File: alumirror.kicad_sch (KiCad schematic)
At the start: 56 parts, among them SW00 PG1350, SW01 PG1350, SW02 PG1350, SW03 PG1350, SW04 PG1350, SW05 PG1350, SW10 PG1350, SW11 PG1350, SW12 PG1350, SW13 PG1350, SW14 PG1350, SW15 PG1350, SW20 PG1350, SW21 PG1350, SW22 PG1350, SW23 PG1350, SW24 PG1350, SW25 PG1350_1½U, SW30 PG1350_1½U, SW31 PG1350/SKQUCAA010, U1 CH552T, U2 CH552T

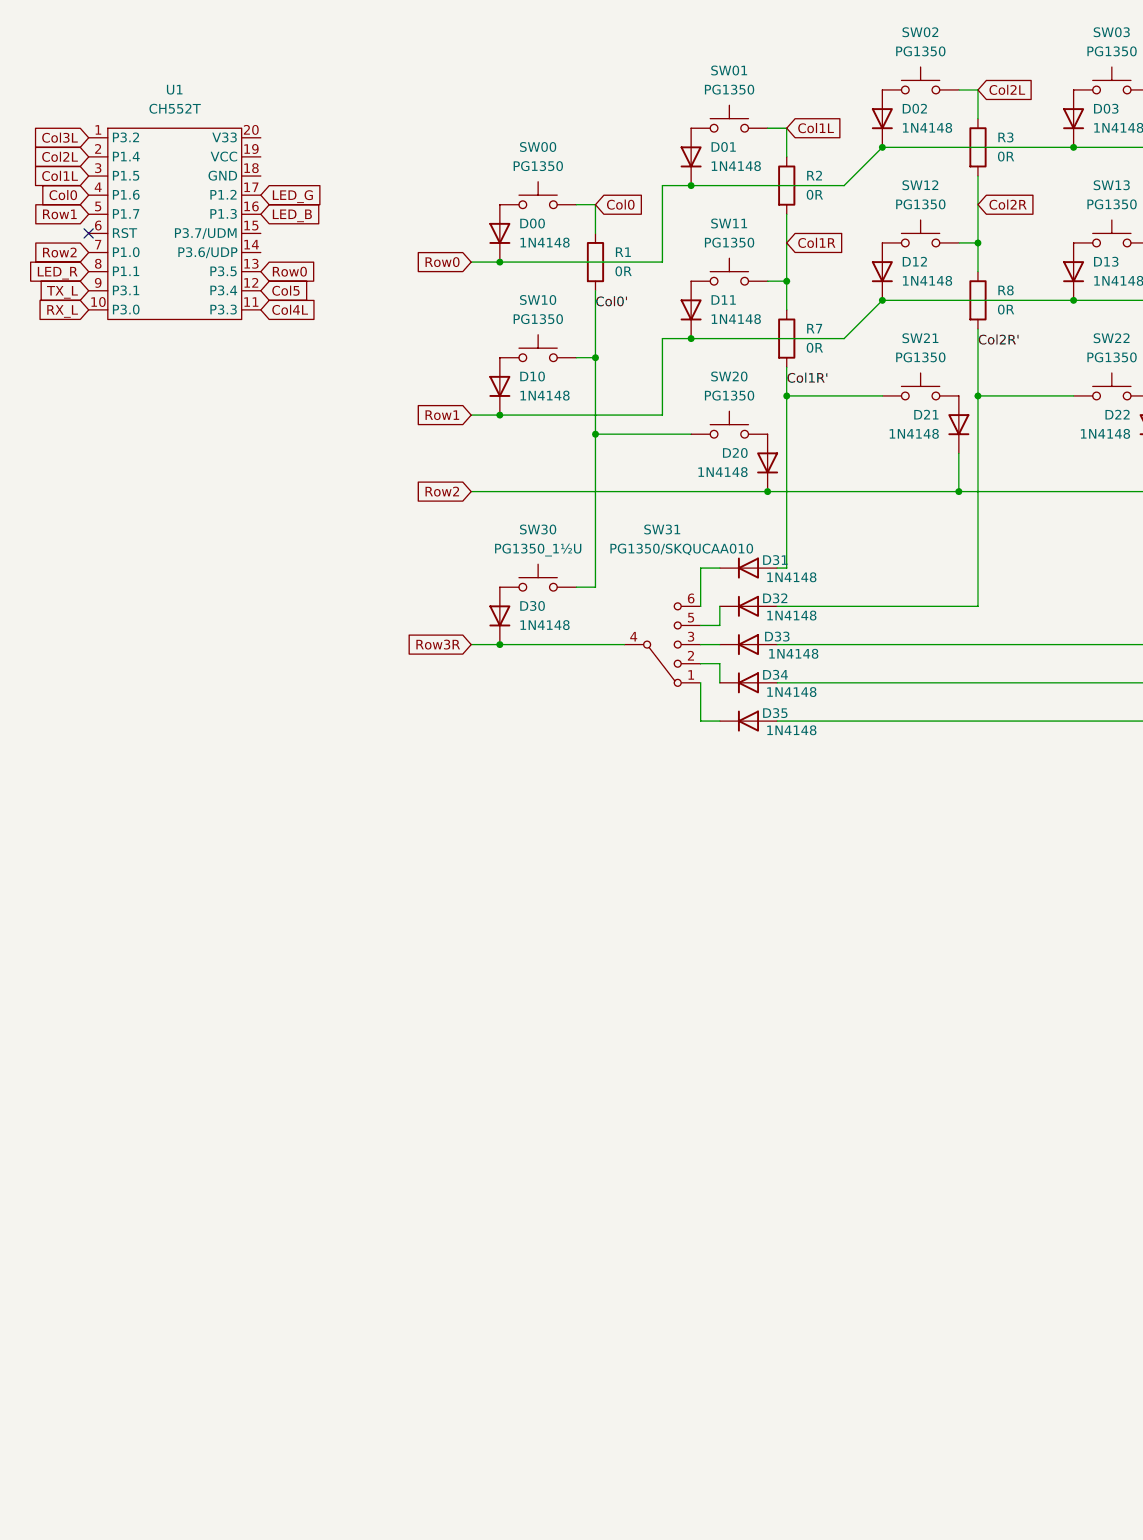
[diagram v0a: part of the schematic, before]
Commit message: Add lefthand USB, ESD, etc. components to schematic
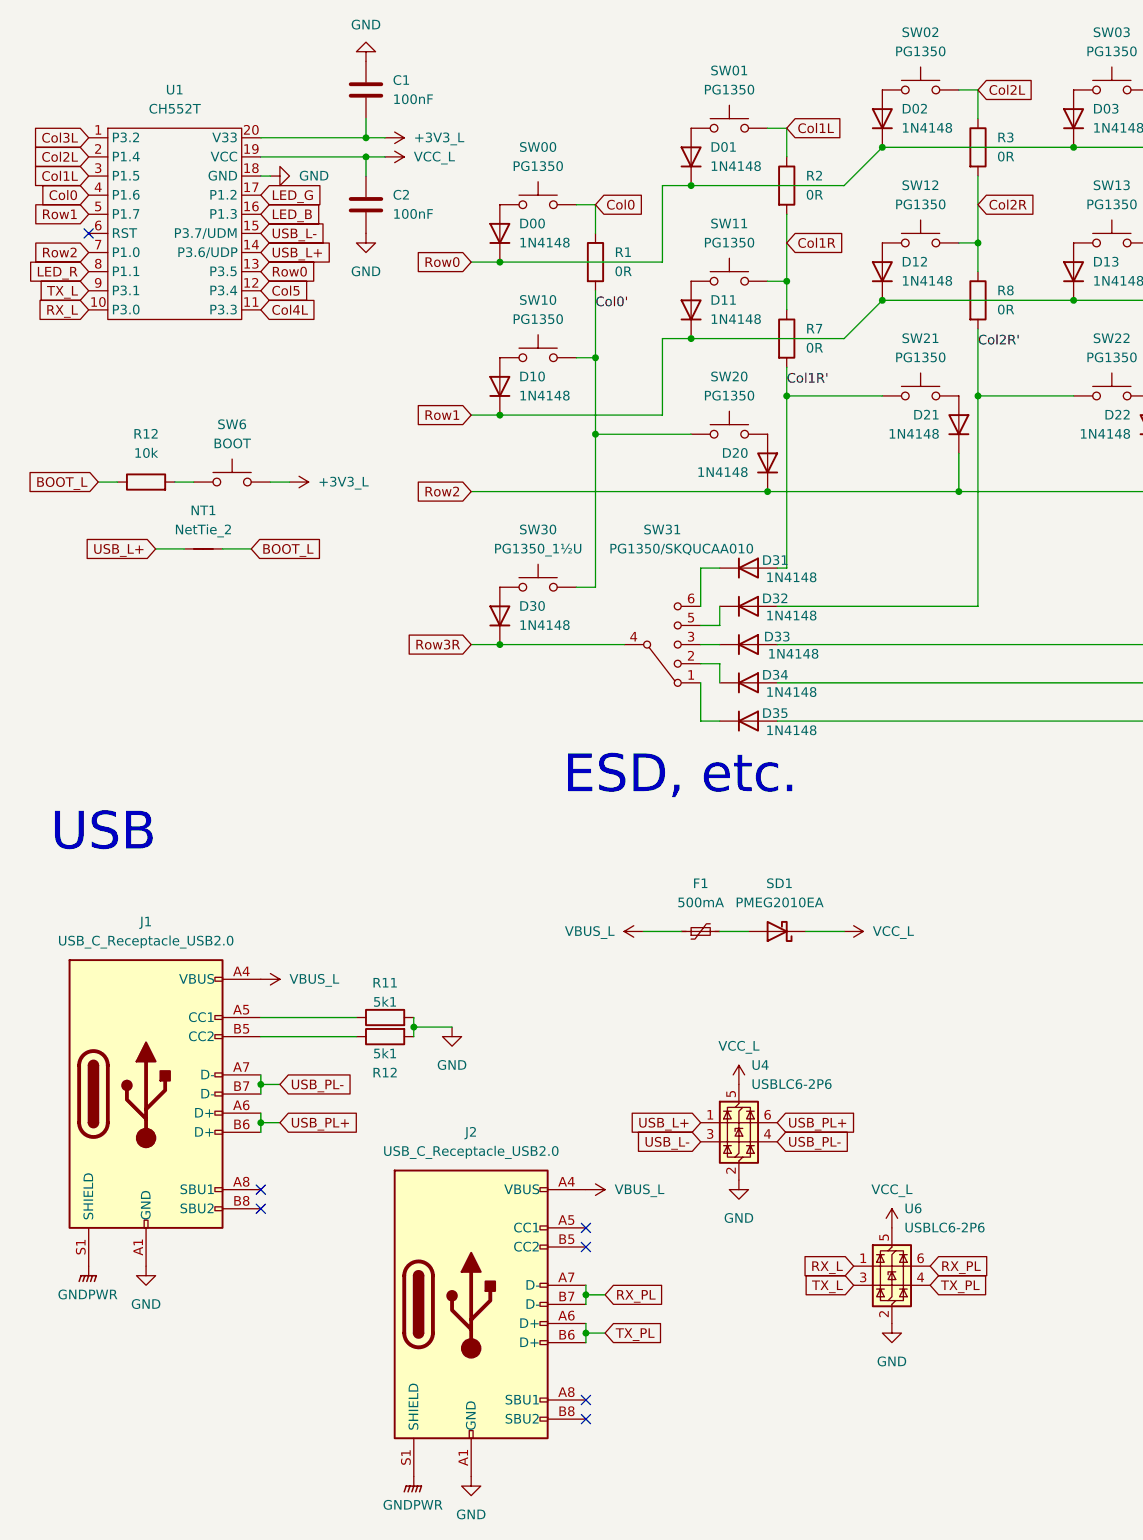
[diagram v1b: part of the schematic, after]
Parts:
- added C1, C2: 100nF, Capacitor_SMD:C_0603_1608Metric, symbol Device:C
- added F1: 500mA, Fuse:Fuse_0603_1608Metric, symbol Device:Polyfuse_Small
- added J1, J2: USB_C_Receptacle_USB2.0, Connector_USB:USB_C_Receptacle_GCT_USB4105-xx-A_16P_TopMnt_Horizontal, symbol Connector:USB_C_Receptacle_USB2.0
- added NT1: NetTie_2, Project Library:NetTie-2_SMD_Pad0.254mm, symbol Device:NetTie_2
- added R11, R12: 5k1, Resistor_SMD:R_0603_1608Metric, symbol Device:R
- added R12: 10k, Resistor_SMD:R_0603_1608Metric, symbol Device:R
- added SD1: PMEG2010EA, Diode_SMD:D_SOD-323, symbol Device:D_Schottky
- added SW6: BOOT, PCM_marbastlib-various:SW_SPST_SKQG_WithStem, symbol Switch:SW_Push
- added U4, U6: USBLC6-2P6, Package_TO_SOT_SMD:SOT-666, symbol Power_Protection:USBLC6-2P6
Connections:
- net RX_L: now also U6.1 (I/O1)
- net TX_L: now also U6.3 (I/O2)
- net USB_L+: now reaches U1.14 (P3.6/UDP)
- net USB_L+: now also NT1.2, U4.1 (I/O1)
- net USB_L-: now reaches U1.15 (P3.7/UDM)
- net USB_L-: now also U4.3 (I/O2)
- net GND: now reaches U1.18 (GND)
- net GND: now also C1.2, C2.2, J1.A1 (GND), J1.A12 (GND), J1.B1 (GND), J1.B12 (GND), J2.A1 (GND), J2.A12 (GND), J2.B1 (GND), J2.B12 (GND), R11.2, R12.2, U4.2 (GND), U6.2 (GND)
- net VCC_L: now reaches U1.19 (VCC)
- net VCC_L: now also C2.1, SD1.1 (K), U4.5 (VBUS), U6.5 (VBUS)
- net +3V3_L: now reaches U1.20 (V33)
- net +3V3_L: now also C1.1, SW6.2
- new net: F1.2, SD1.2 (A)
- new net: J1.A5 (CC1), R11.1
- new net: J1.B5 (CC2), R12.1
- new net: R12.2, SW6.1
- new net BOOT_L: NT1.1, R12.1
- new net GNDPWR: J1.S1 (SHIELD), J2.S1 (SHIELD)
- new net RX_PL: J2.A7 (D-), J2.B7 (D-), U6.6 (I/O1)
- new net TX_PL: J2.A6 (D+), J2.B6 (D+), U6.4 (I/O2)
- new net USB_PL+: J1.A6 (D+), J1.B6 (D+), U4.6 (I/O1)
- new net USB_PL-: J1.A7 (D-), J1.B7 (D-), U4.4 (I/O2)
- new net VBUS_L: F1.1, J1.A4 (VBUS), J1.A9 (VBUS), J1.B4 (VBUS), J1.B9 (VBUS), J2.A4 (VBUS), J2.A9 (VBUS), J2.B4 (VBUS), J2.B9 (VBUS)
- no-connect marks 2 -> 8
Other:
- note added: "ESD, etc."
- note added: "USB"

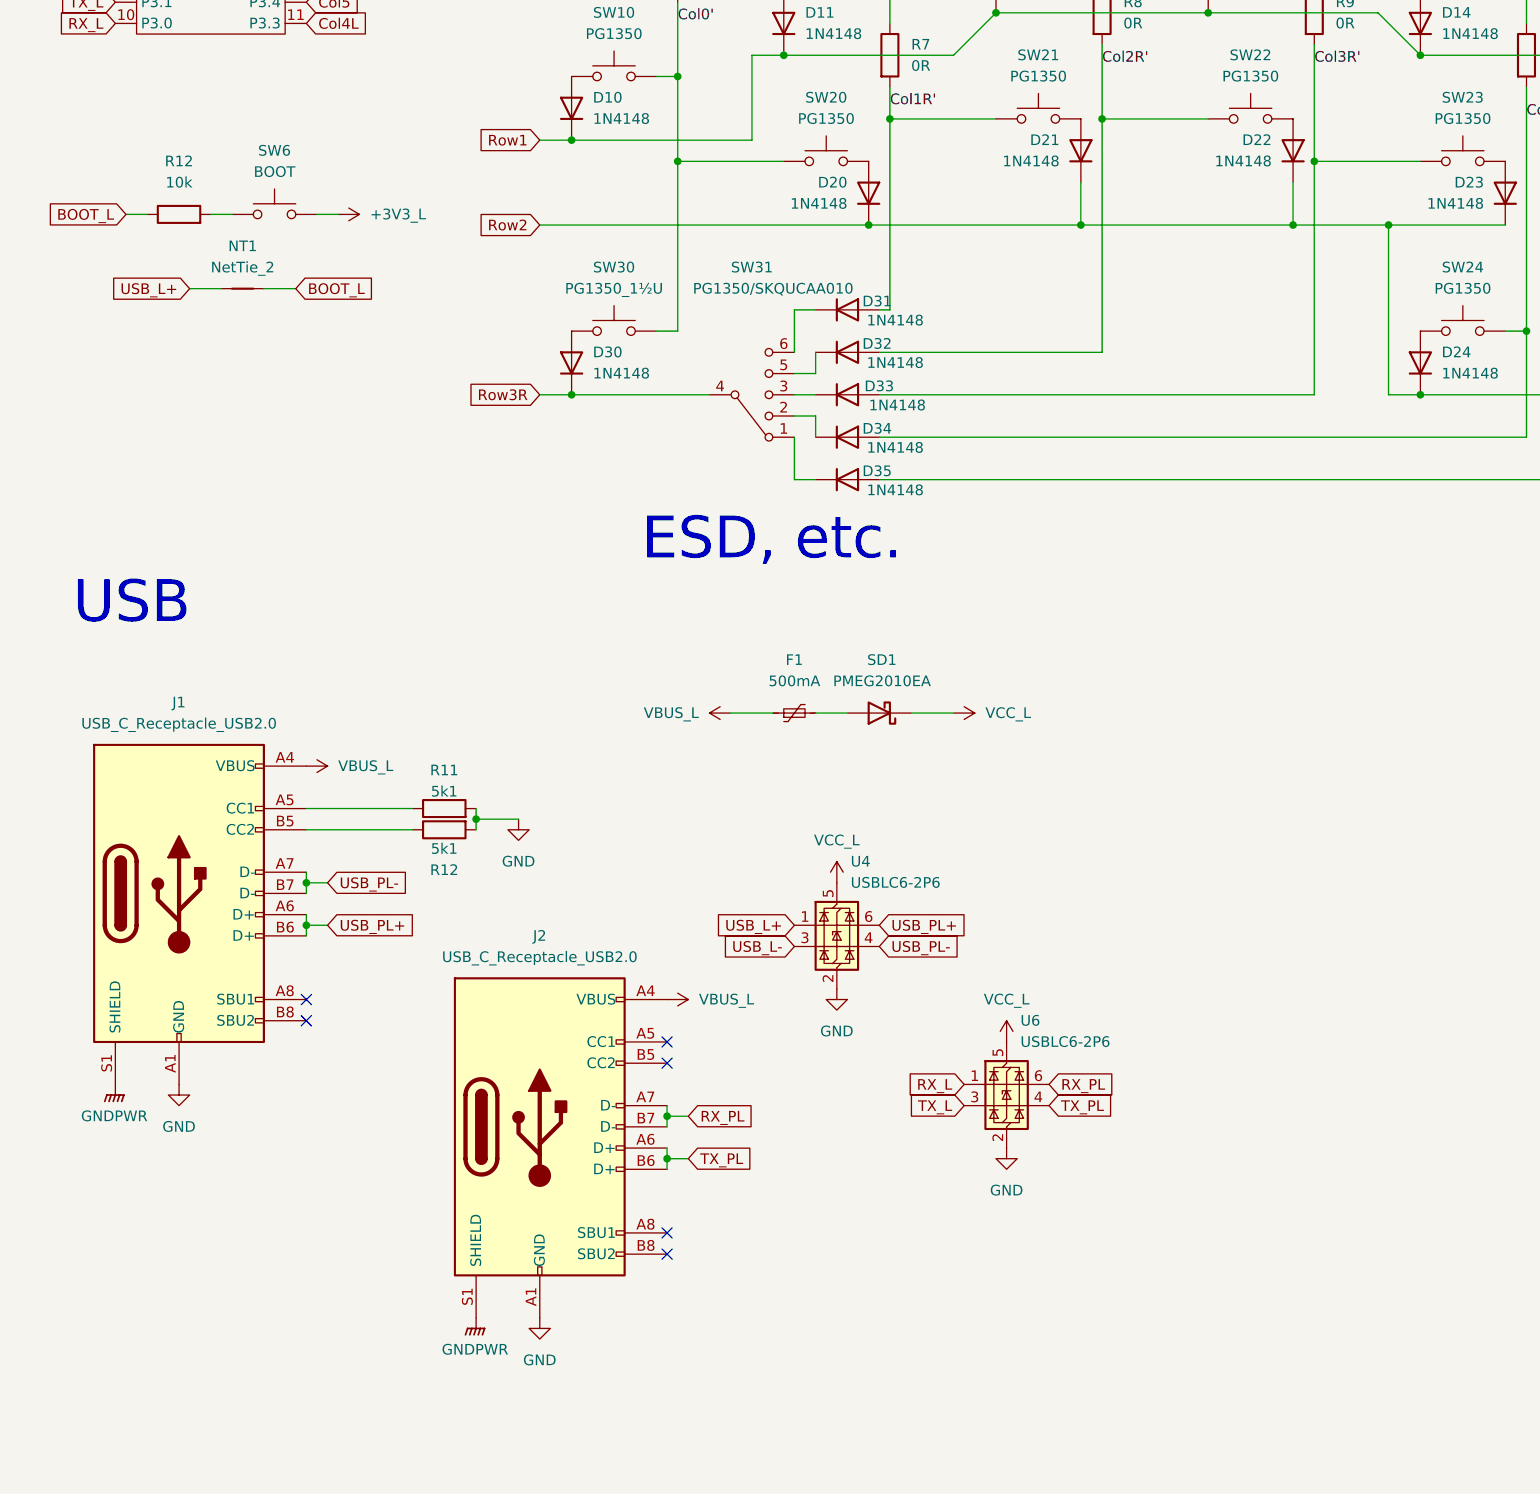
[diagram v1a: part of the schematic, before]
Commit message: Add lefthand active components to PCB and route
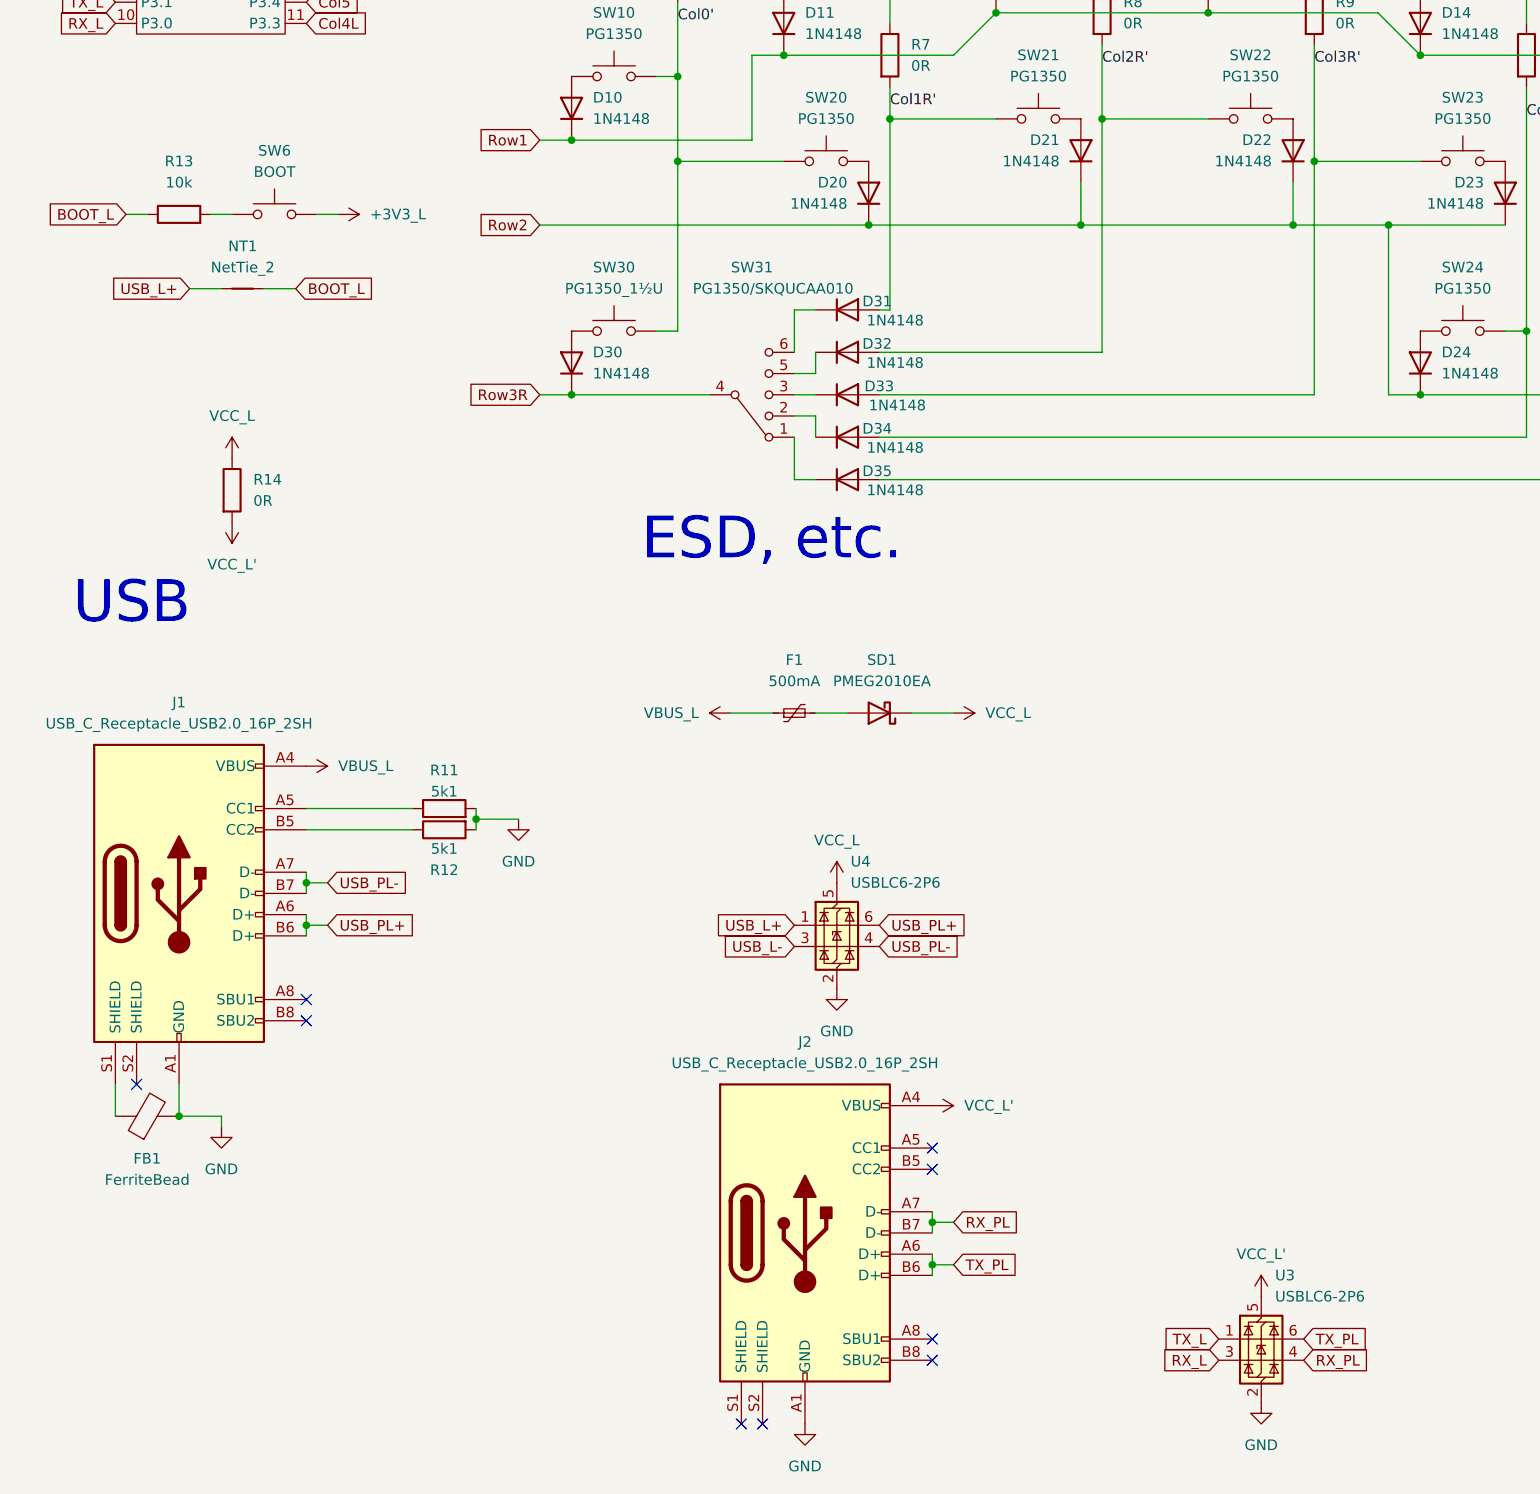
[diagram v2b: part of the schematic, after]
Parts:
- removed J1, J2: USB_C_Receptacle_USB2.0, Connector_USB:USB_C_Receptacle_GCT_USB4105-xx-A_16P_TopMnt_Horizontal, symbol Connector:USB_C_Receptacle_USB2.0
- removed U6: USBLC6-2P6, Package_TO_SOT_SMD:SOT-666, symbol Power_Protection:USBLC6-2P6
- added FB1: FerriteBead, Inductor_SMD:L_0805_2012Metric, symbol Device:FerriteBead
- added J1, J2: USB_C_Receptacle_USB2.0_16P_2SH, Project Library:USB_C_Receptacle_HRO_TYPE-C-31-M-12, symbol Project Library:USB_C_Receptacle_USB2.0_16P_2SH
- added R14: 0R, Project Library:R_2010_5025Metric_Mod, symbol Device:R
- added U3: USBLC6-2P6, Package_TO_SOT_SMD:SOT-666, symbol Power_Protection:USBLC6-2P6
- NT1: footprint Project Library:NetTie-2_SMD_Pad0.254mm -> Project Library:NetTie-2_SMD_Pad0.2mm
- SW6: footprint PCM_marbastlib-various:SW_SPST_SKQG_WithStem -> Project Library:SW_SPST_SKQG_WithStem
- renumbered R12 to R13
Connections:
- net GND: now also FB1.2, J1.A1 (GND), J1.A12 (GND), J1.B1 (GND), J1.B12 (GND), J2.A1 (GND), J2.A12 (GND), J2.B1 (GND), J2.B12 (GND), U3.2 (GND)
- net RX_L: now also U3.3 (I/O2)
- net RX_PL: now also J2.A7 (D-), J2.B7 (D-), U3.4 (I/O2)
- net TX_L: now also U3.1 (I/O1)
- net TX_PL: now also J2.A6 (D+), J2.B6 (D+), U3.6 (I/O1)
- net USB_PL+: now also J1.A6 (D+), J1.B6 (D+)
- net USB_PL-: now also J1.A7 (D-), J1.B7 (D-)
- net VBUS_L: now also J1.A4 (VBUS), J1.A9 (VBUS), J1.B4 (VBUS), J1.B9 (VBUS)
- net VCC_L: now also R14.1
- net at R11.1: now also J1.A5 (CC1)
- net at R12.1: now also J1.B5 (CC2)
- new net: FB1.1, J1.S1 (SHIELD)
- new net VCC_L': J2.A4 (VBUS), J2.A9 (VBUS), J2.B4 (VBUS), J2.B9 (VBUS), R14.2, U3.5 (VBUS)
- no-connect marks 8 -> 11
